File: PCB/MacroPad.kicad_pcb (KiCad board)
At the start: 2 copper layers, 61.6 x 69.2 mm, 11 parts, among them SW1 SW_Push, SW2 SW_Push, SW3 SW_Push, SW4 SW_Push, SW5 SW_Push, SW6 SW_Push, U1 XIAO-RP2040-DIP

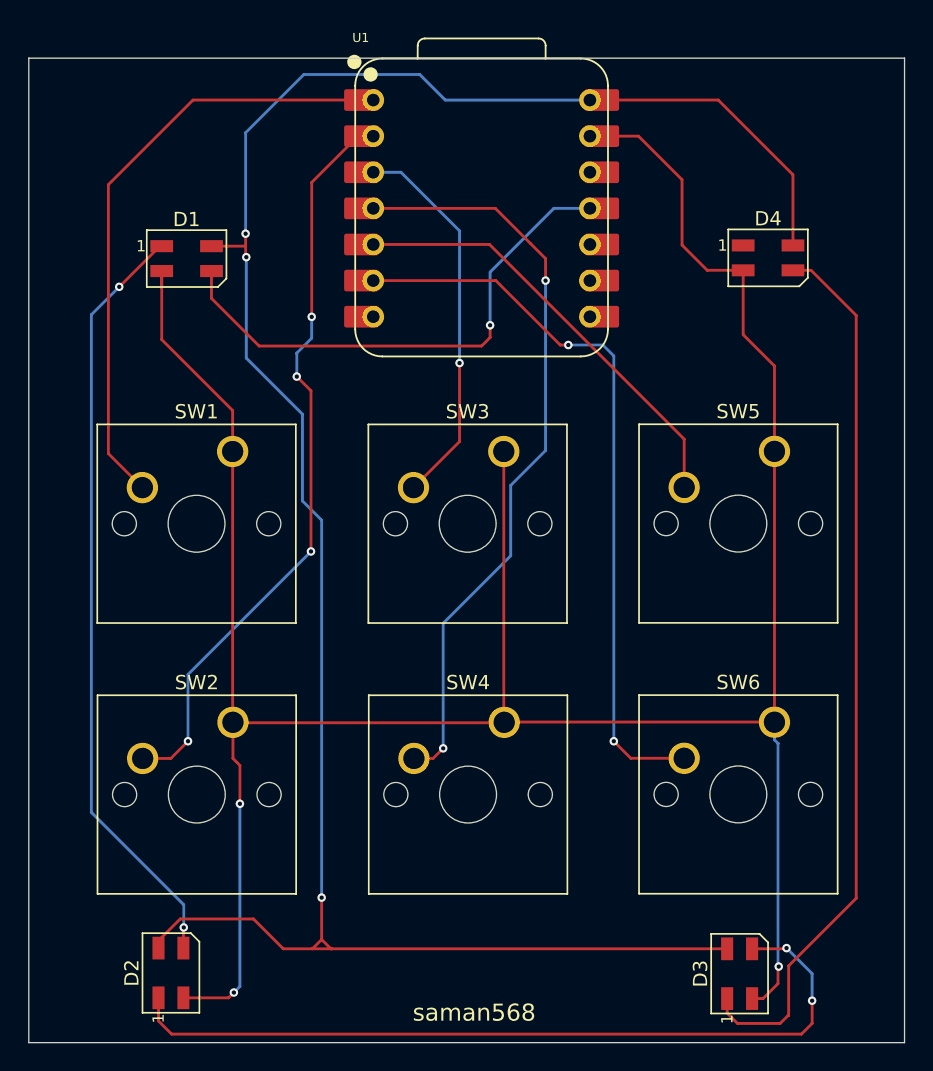
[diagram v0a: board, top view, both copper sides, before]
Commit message: fixed wrong footprint for SK6812MINI-E
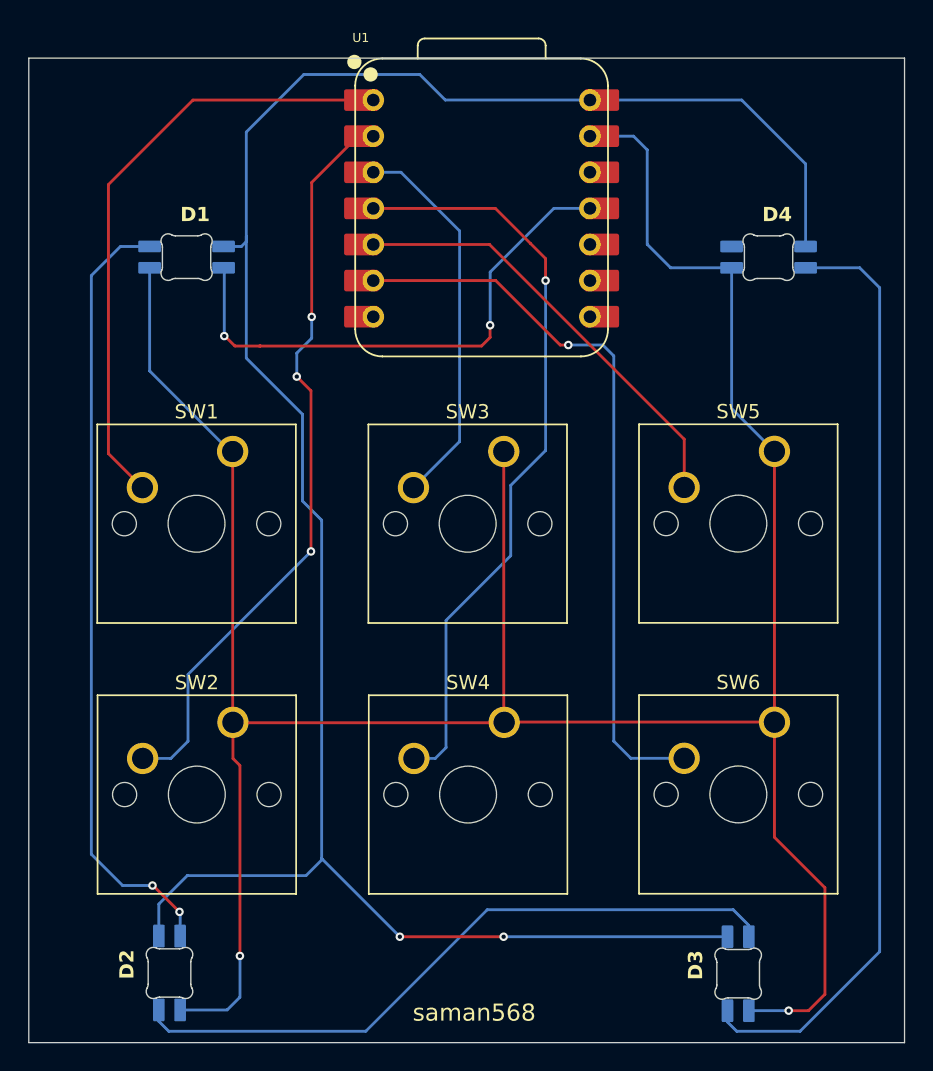
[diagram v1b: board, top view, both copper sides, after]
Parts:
- D1: value SK6812MINI -> MINI-E:SK6812MINI-E_fixed; footprint LED_SMD:LED_SK6812MINI_PLCC4_3.5x3.5mm_P1.75mm -> MINI-E:SK6812MINI-E_fixed
- D2, D3, D4: footprint LED_SMD:LED_SK6812MINI_PLCC4_3.5x3.5mm_P1.75mm -> MINI-E:SK6812MINI-E_fixed
- moved D4 0.06 mm to (152.9, 35.3)
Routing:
- net Net-(D2-DOUT): track 56.8 -> 47.4 mm, vias 2 -> 0
- net GND: track 186.2 -> 193.2 mm, vias 3 -> 2
- net Net-(D3-DOUT): track 62.9 -> 66.6 mm
- net Net-(D1-VDD): track 152.5 -> 150.7 mm, vias 3 -> 2
- net Net-(D1-DIN): track 36.6 -> 37.7 mm, vias 1 -> 2
- net Net-(D1-DOUT): track 54.2 -> 55.2 mm
- net Net-(U1-GPIO29/ADC3/A3): track 53.4 -> 53.5 mm, vias 2 -> 1
- net Net-(U1-GPIO7/SCL): vias 2 -> 1
- net Net-(U1-GPIO28/ADC2/A2): vias 1 -> 0
- net Net-(U1-GPIO27/ADC1/A1): vias 4 -> 3
